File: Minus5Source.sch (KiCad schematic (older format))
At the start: 7 parts, among them U5 LM27761

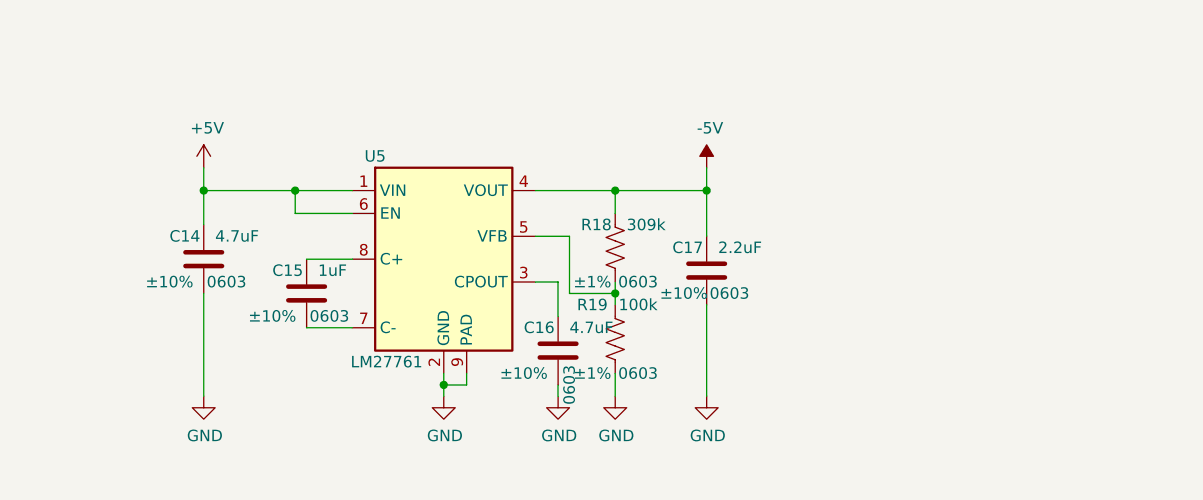
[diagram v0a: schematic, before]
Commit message: Adding the LP filter to the level shifter
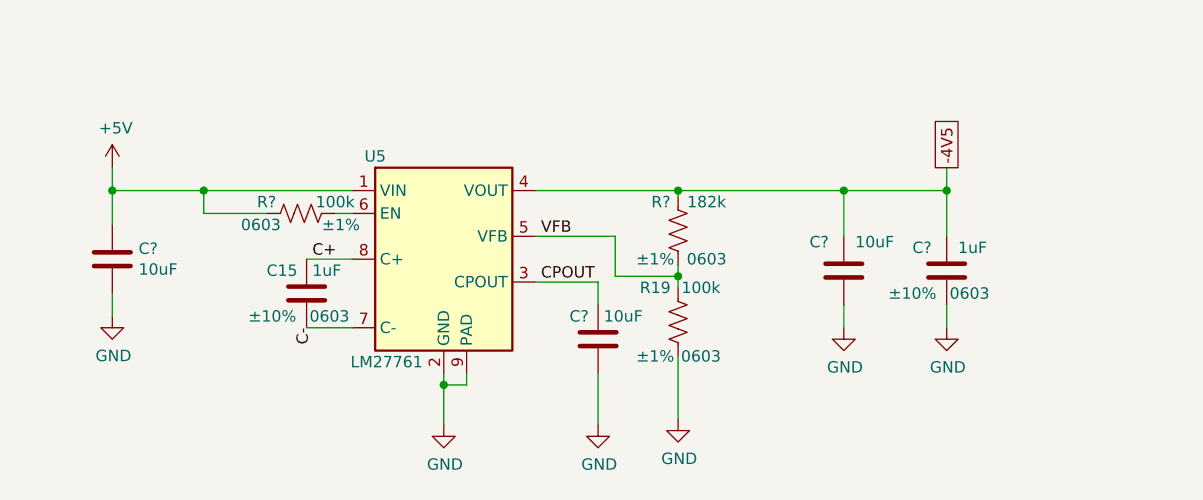
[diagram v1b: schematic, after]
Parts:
- removed C14, C16: 4.7uF, Capacitor_SMD:C_0603_1608Metric, symbol Device:C
- removed C17: 2.2uF, Capacitor_SMD:C_0603_1608Metric, symbol Device:C
- removed R18: 309k, Resistor_SMD:R_0603_1608Metric, symbol Device:R_US
- added C?: 1uF, Capacitor_SMD:C_0603_1608Metric, symbol Device:C
- added C? (x3): 10uF, symbol Device:C
- added R?: 100k, Resistor_SMD:R_0603_1608Metric, symbol Device:R_US
- added R?: 182k, Resistor_SMD:R_0603_1608Metric, symbol Device:R_US
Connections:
- net +5V: now also C?.1, R?.2; no longer U5.6 (EN)
- net GND: now also C?.1, C?.2, C?.2, C?.2
- net CPOUT: now reaches U5.3 (CPOUT)
- net CPOUT: now also C?.1
- net VFB: now reaches R19.1, U5.5 (VFB)
- net VFB: now also R?.2
- net C-: now reaches C15.1, U5.7 (C-)
- net C+: now reaches C15.2, U5.8 (C+)
- net -5V renamed -4V5
- net -4V5: now also C?.1, C?.2, R?.1
- new net: R?.1, U5.6 (EN)
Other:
- moved on the sheet: R19

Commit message: Finalized rev dev.a.2 with improved filtering, power supply design, and silkscreen
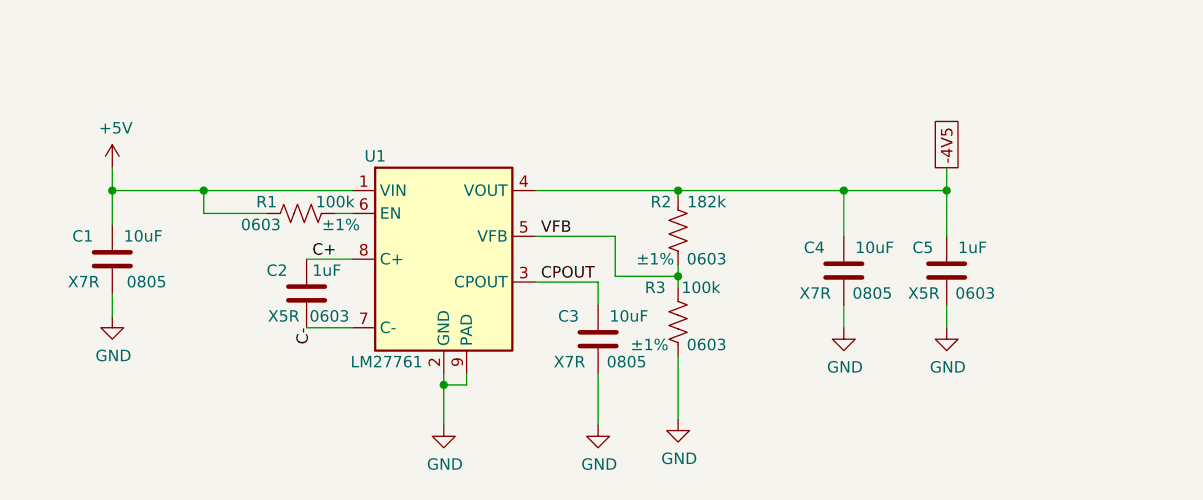
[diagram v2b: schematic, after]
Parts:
- removed C? (x2): 10uF, symbol Device:C
- added C3, C4: 10uF, Capacitor_SMD:C_0805_2012Metric, symbol Device:C
- C1: renamed from C?; footprint (none) -> Capacitor_SMD:C_0805_2012Metric; DK_Detail_Page (none) -> https://www.digikey.com/en/products/detail/samsung-electro-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; Description (none) -> CAP CER 10UF 10V X7R 0805; Digi-Key_PN (none) -> 1276-1764-1-ND; MPN (none) -> CL21B106KPQNNNE; Manufacturer (none) -> Samsung Electro-Mechanics; Package (none) -> 0805; Temperature Coefficient (none) -> X7R; Tolerance (none) -> ±10%
- R1: renamed from R?; Digi-Key Part Number 311-100KHRCT-ND -> (none); Digi-Key_PN (none) -> 311-100KHRCT-ND
- R2: renamed from R?; DK_Detail_Page https://www.digikey.com/en/products/detail/yageo/RC0603FR-07100KL/726889 -> https://www.digikey.com/en/products/detail/yageo/RC0603FR-07182KL/726997; Digi-Key Part Number 311-100KHRCT-ND -> (none); Digi-Key_PN (none) -> 311-182KHRCT-ND
- R3: renamed from R19; Digi-Key Part Number 311-100KHRCT-ND -> (none); Digi-Key_PN (none) -> 311-100KHRCT-ND
- gave numbers to parts that had none: 1
- renumbered C15 to C2, U5 to U1
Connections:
- net -4V5: now also C4.1
- net CPOUT: now also C3.1
- net GND: now also C3.2, C4.2

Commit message: Major overhaul given chip shortage. Completely redid the power supply, and refined the amps for the EMG to give better gain and use the full output range
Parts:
- removed C5: 1uF, Capacitor_SMD:C_0603_1608Metric, symbol Device:C
- removed R1, R3: 100k, Resistor_SMD:R_0603_1608Metric, symbol Device:R_US
- removed R2: 182k, Resistor_SMD:R_0603_1608Metric, symbol Device:R_US
- removed U1: LM27761, Package_SON:WSON-8-1EP_2x2mm_P0.5mm_EP0.9x1.6mm, symbol Regulator_SwitchedCapacitor:LM27761
- added C?: 1uF, Capacitor_SMD:C_0805_2012Metric, symbol Device:C
- added TP1: -3V, digikey-footprints:Test_Point_D1.02mm, symbol dk_Test-Points:5011
- added U1: TPS60403, Package_TO_SOT_SMD:SOT-23-5, symbol FANTM_parts:TPS60403
- added U2: MAX1735, Package_TO_SOT_SMD:SOT-23-5, symbol FANTM_parts:MAX1735
- C1, C3, C4: value 10uF -> 1uF; DK_Detail_Page https://www.digikey.com/en/products/detail/samsung-electro-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 -> (none); Description CAP CER 10UF 10V X7R 0805 -> CAP CER 1UF 16V X7R 0805; Digi-Key_PN 1276-1764-1-ND -> 1276-6471-1-ND; MPN CL21B106KPQNNNE -> CL21B105KOFNNNG; Tolerance ±10% -> (none); Voltage Rating (none) -> 16V
- C2: footprint Capacitor_SMD:C_0603_1608Metric -> Capacitor_SMD:C_0805_2012Metric;  Temperature Coefficient X5R -> (none); Description (none) -> CAP CER 1UF 16V X7R 0805; Digi-Key_PN 1276-1034-1-ND -> 1276-6471-1-ND; MPN (none) -> CL21B105KOFNNNG; Manufacturer (none) -> Samsung Electro-Mechanics; Package 0603 -> 0805; Temperature Coefficient (none) -> X7R; Tolerance ±10% -> (none); Voltage Rating (none) -> 16V
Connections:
- net labels added: -3V, -5V, Cfly+, Cfly-
- net labels removed: -4V5, C+, C-, CPOUT, VFB
- wire segments 32 -> 26

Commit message: Fixed SPI signal naming convention to new OSHWA proposal
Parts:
- gave numbers to parts that had none: 1
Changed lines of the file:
@@
 	4375 1850 4375 1700
 $Comp
-L Device:C C?
+L Device:C C13
 U 1 1 608D2D70
 P 2750 2075
-F 0 "C?" H 2850 1975 50  0000 C CNN
+F 0 "C13" H 2850 1975 50  0000 C CNN
 F 1 "1uF" H 2625 1975 50  0000 C CNN
 F 2 "Capacitor_SMD:C_0805_2012Metric" H 2788 1925 50  0001 C CNN
@@
 P 2750 2275
 AR Path="/6043E029/608D4C88" Ref="#PWR?"  Part="1"
-AR Path="/605EF1AE/608D4C88" Ref="#PWR?"  Part="1"
-F 0 "#PWR?" H 2750 2025 50  0001 C CNN
+AR Path="/605EF1AE/608D4C88" Ref="#PWR0101"  Part="1"
+F 0 "#PWR0101" H 2750 2025 50  0001 C CNN
 F 1 "GND" H 2755 2102 50  0000 C CNN
 F 2 "" H 2750 2275 50  0001 C CNN

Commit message: Finished rev dev.a.4 with safety improvements, better gain settings, and dc offset removal
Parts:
- added C4: 0.1uF, Capacitor_SMD:C_0603_1608Metric, symbol Device:C
- added R1: 249, Resistor_SMD:R_0603_1608Metric, symbol Device:R_US
- C1, C2, C3: value 1uF -> 3.3uF; Description CAP CER 1UF 16V X7R 0805 -> CAP CER 3.3UF 10V X5R 0805; Digi-Key_PN 1276-6471-1-ND -> 1276-2912-1-ND; Temperature Coefficient X7R -> X5R; Voltage Rating 16V -> 10V
- U1: value TPS60403 -> TPS60402; Current 60mA -> MAX: 20mA; Digi-Key_PN 296-18036-1-ND -> 296-31988-1-ND; MPN TPS60403QDBVRQ1 -> TPS60402DBVR
- renumbered C13 to C5, C4 to C6, TP1 to TP3
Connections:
- net labels added: INV_OUT, LDO_IN
- net labels removed: -5V
- wire segments 26 -> 30
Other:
- moved on the sheet: C5, C6
